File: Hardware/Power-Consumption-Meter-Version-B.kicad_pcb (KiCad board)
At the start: 2 copper layers, 90 x 96.5 mm, 35 parts, among them J1 Jack_DC, J10 01x02, J11 01x02, J12 01x02, J13 01x02, J2 BAT_IN, J3 PWR_BTN, J4 USB_A, J5 Jack_DC, J6 Jack_DC, J7 USB_B_Mini, J8 USB_B_Micro, J9 01x04, SW1 SW_Slide, SW2 SW_Push, U1 Arduino_Nano_v3.x, U2 Display_5641BS, U3 INA219_Module

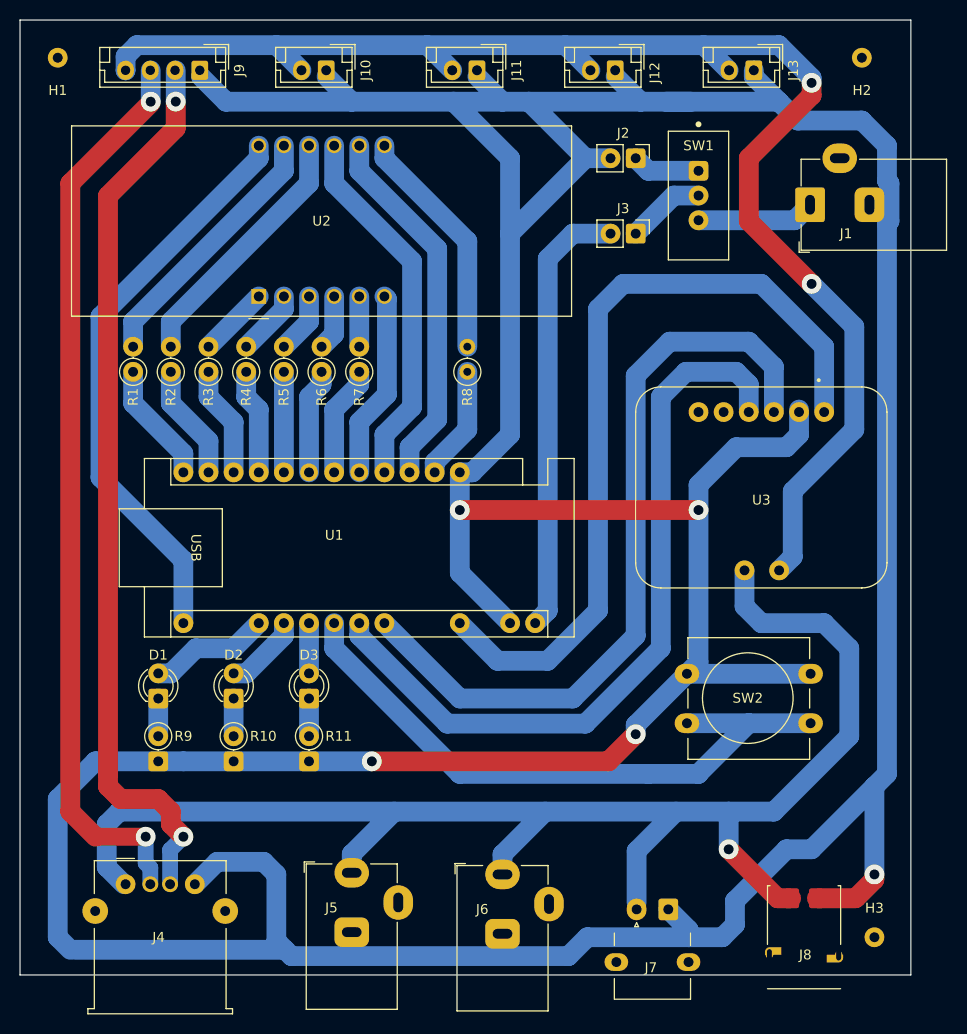
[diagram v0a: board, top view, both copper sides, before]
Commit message: Version B: adding case 3D model
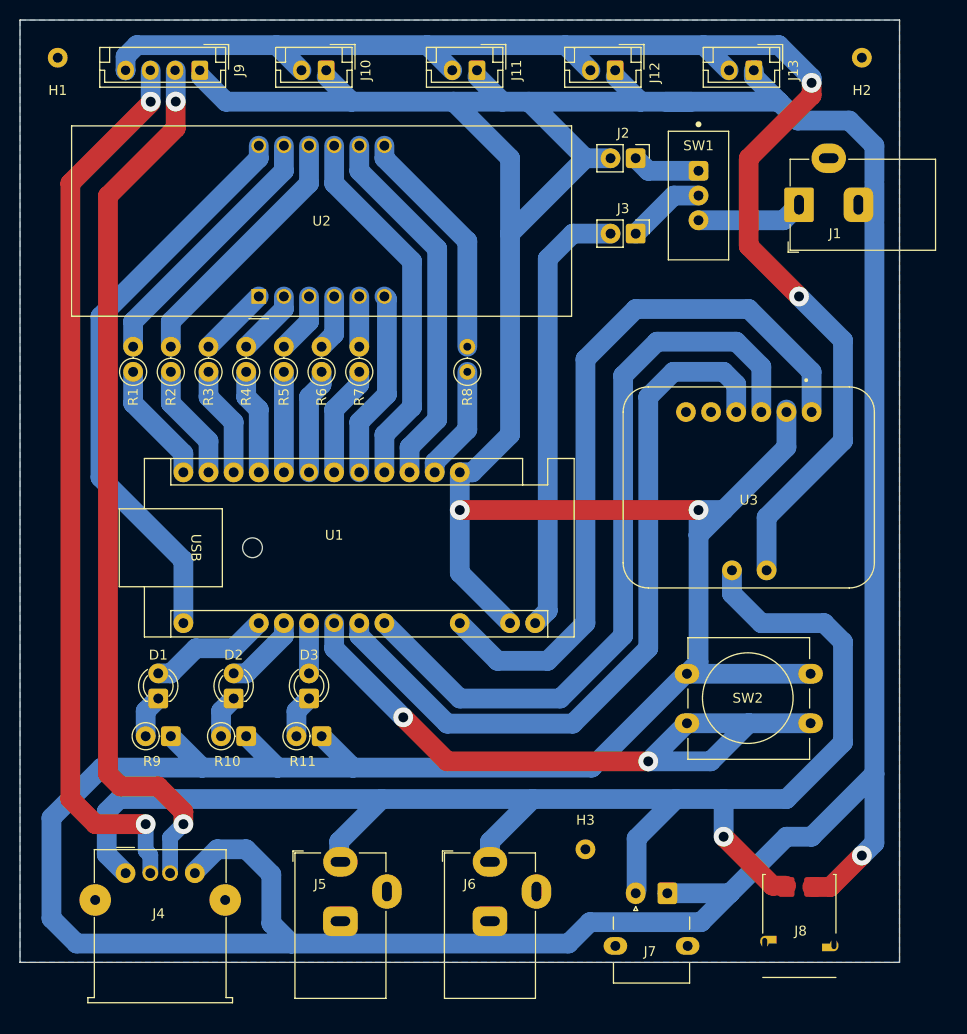
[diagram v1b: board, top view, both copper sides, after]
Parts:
- added H4: MountingHole, MountingHole:MountingHole_2mm, F.Cu at (120.0, 86.4)
- J3: value PWR_BTN -> ON_OFF
- SW1: value SW_Slide -> PWR_SW
- moved H3 30.5 mm to (153.7, 116.8)
- moved J6 1.80 mm to (144.0, 118.1)
- moved J7 1.63 mm to (158.8, 121.6)
- moved J5 1.59 mm to (128.9, 118.1)
- moved R11 1.27 mm to (124.5, 105.4), turned to 0 degrees
- moved R10 1.27 mm to (116.8, 105.4), turned to 0 degrees
- moved R9 1.27 mm to (109.2, 105.4), turned to 0 degrees
- moved U3 1.27 mm to (170.2, 80.3)
- moved J8 1.24 mm to (175.3, 126.4)
- moved J4 1.12 mm to (107.2, 119.3)
- moved J1 1.11 mm to (175.3, 51.7)
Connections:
- J1 pad 3: (no net) -> unconnected-(J1-MountPin-Pad3)
- J5 pad 3: (no net) -> unconnected-(J5-MountPin-Pad3)
- J6 pad 3: (no net) -> unconnected-(J6-MountPin-Pad3)
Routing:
- net GND: track 519.8 -> 529.7 mm, vias 5 -> 3
- net 5V: track 81.0 -> 73.9 mm
- net Net-(U1-A3): track 64.4 -> 68.8 mm, vias 0 -> 2
- net I2C_SDA: track 77.0 -> 75.7 mm
- net I2C_SCL: track 78.2 -> 77.0 mm
- net DATA1+: track 91.1 -> 89.8 mm
- net DATA1-: track 92.0 -> 90.7 mm
- net Net-(J1-Pad1): track 11.9 -> 10.8 mm
- net Net-(D3-K): track 3.81 -> 4.34 mm
- net Net-(D2-K): track 3.81 -> 4.34 mm
- net Net-(D1-K): track 3.81 -> 4.34 mm
- net VIN+: track 149.6 -> 149.0 mm
- added copper zone on B.Cu, net GND
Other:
- board size 90 x 96.5 mm -> 88.9 x 95.2 mm
